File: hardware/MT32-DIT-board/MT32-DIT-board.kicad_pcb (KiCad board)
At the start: 2 copper layers, 35 x 35 mm, 47 parts, among them J1 I2S_CONN, J2 spdif_dit, J3 spdif_wm, T1 PE-65612NL, U1 DIT4192IPW, U2 WM8804

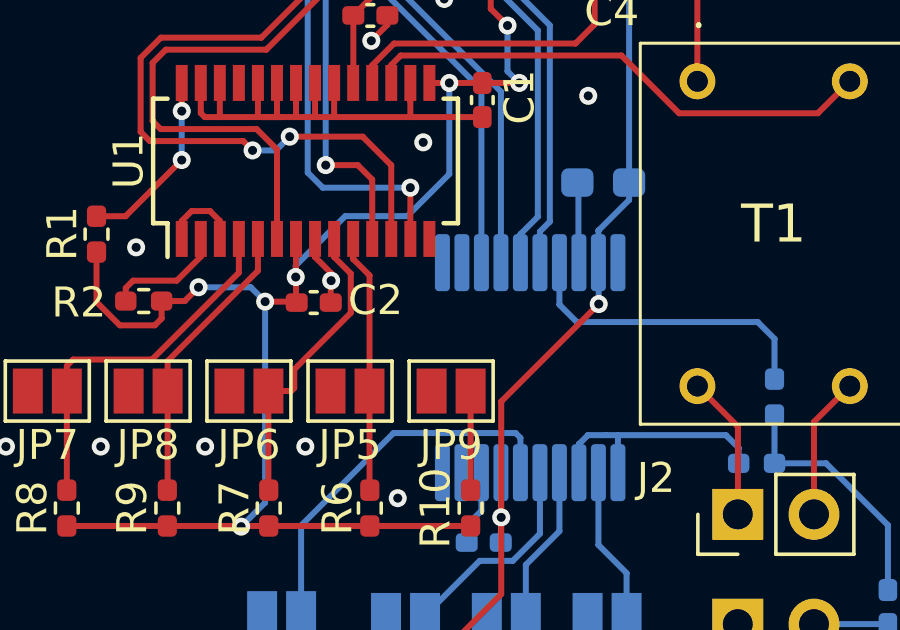
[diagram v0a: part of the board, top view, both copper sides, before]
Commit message: M/S pin was not connected due to Kicad terrible grid, fixed
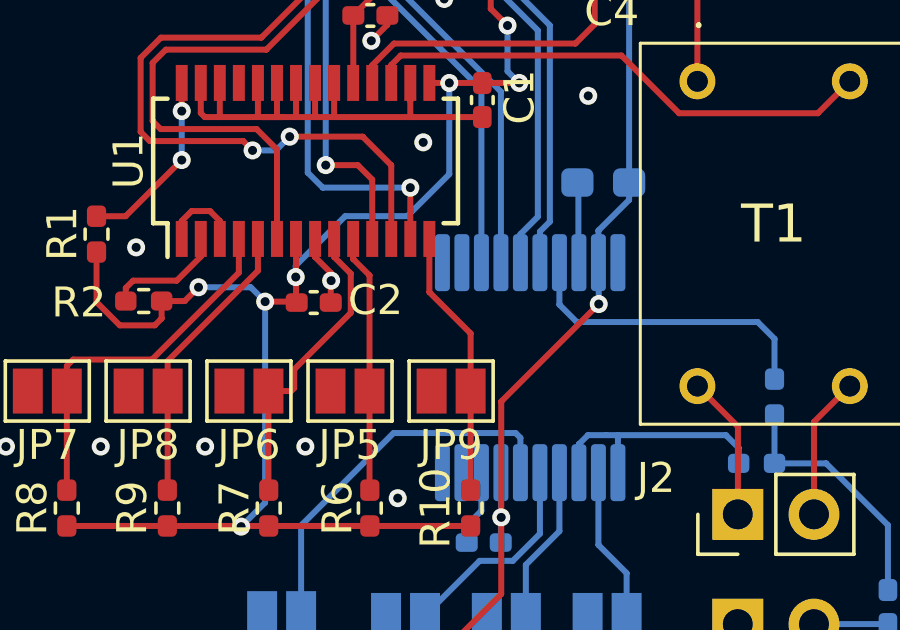
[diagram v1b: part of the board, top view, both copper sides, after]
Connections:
- JP5 pad 2: GNDREF -> Net-(JP5-B)
- JP6 pad 2: GNDREF -> Net-(JP5-B)
- JP7 pad 2: GNDREF -> Net-(JP5-B)
- JP9 pad 1: Net-(JP9-A) -> M/S
- R10 pad 2: Net-(JP9-A) -> M/S
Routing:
- net M/S: track 0.00 -> 8.94 mm
- net Net-(JP9-A): track 3.30 -> 0.00 mm

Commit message: Kicad 9.0.5 update
Kicad update to 9.0.5
Src change: dtr is back, second buffer register added
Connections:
- JP5 pad 2: Net-(JP5-B) -> GNDREF
- JP6 pad 2: Net-(JP5-B) -> GNDREF
- JP7 pad 2: Net-(JP5-B) -> GNDREF
